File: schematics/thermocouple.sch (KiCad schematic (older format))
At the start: 0 parts

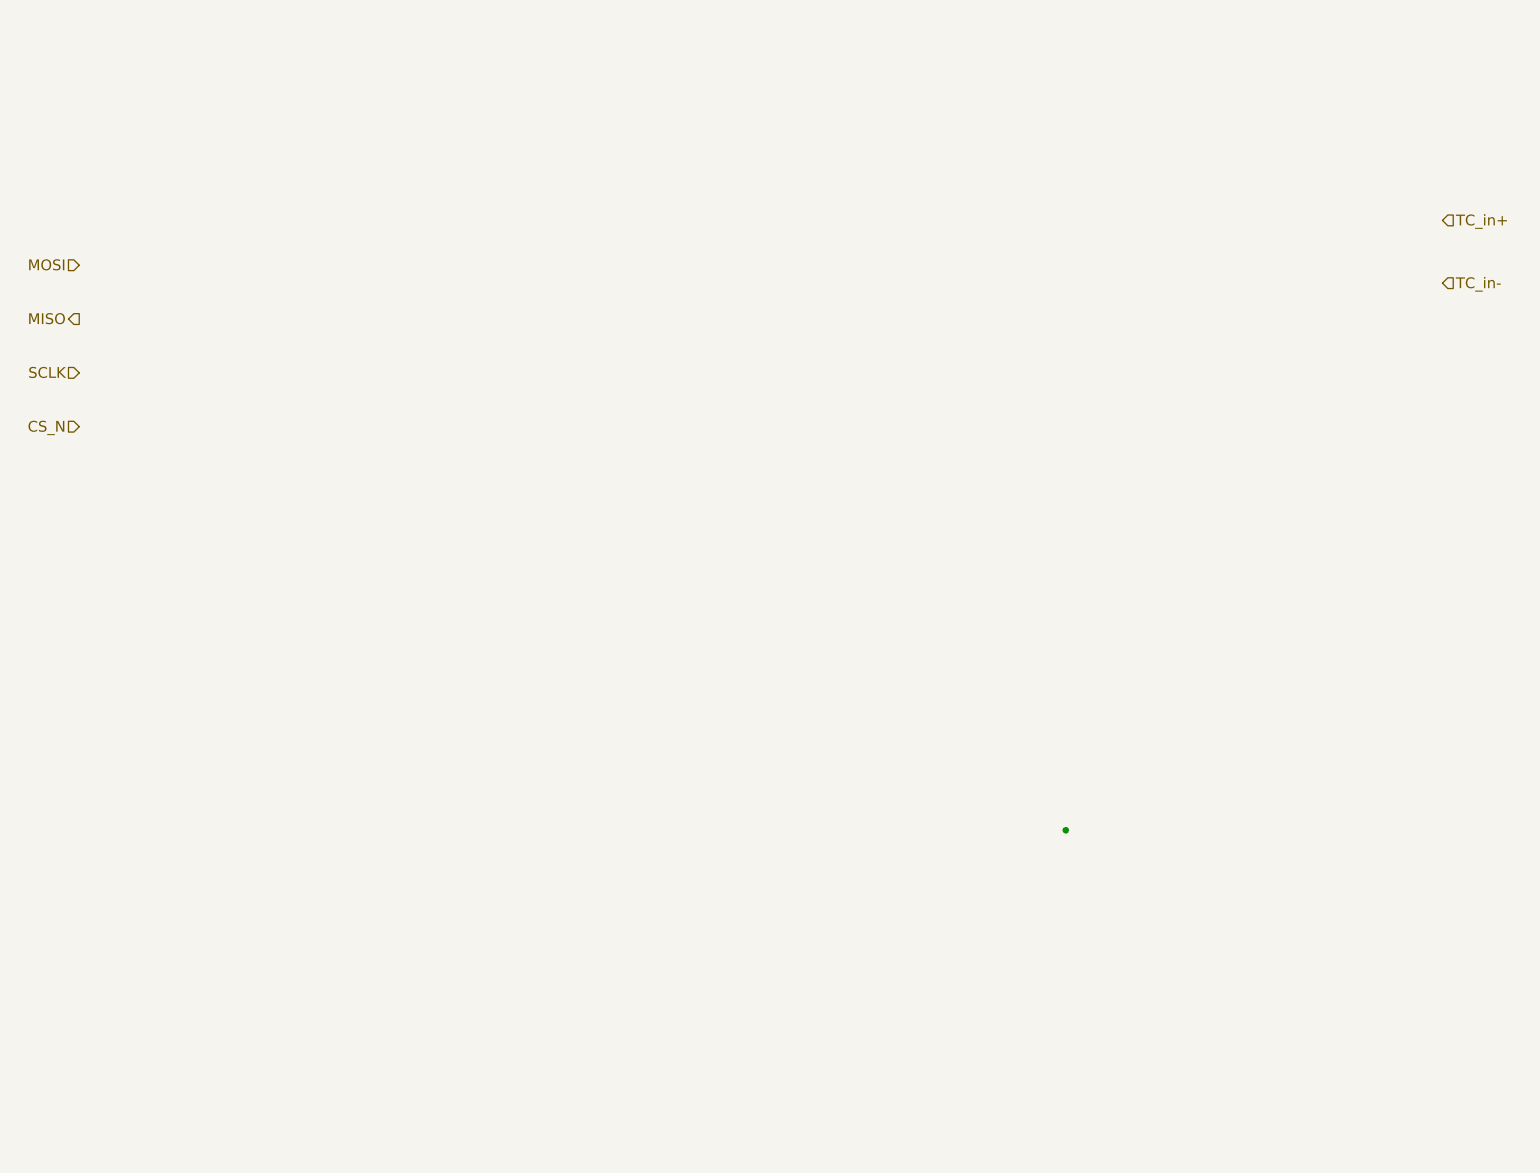
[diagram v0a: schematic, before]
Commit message: added fake diff amp and temp adc to thermocouple circuit
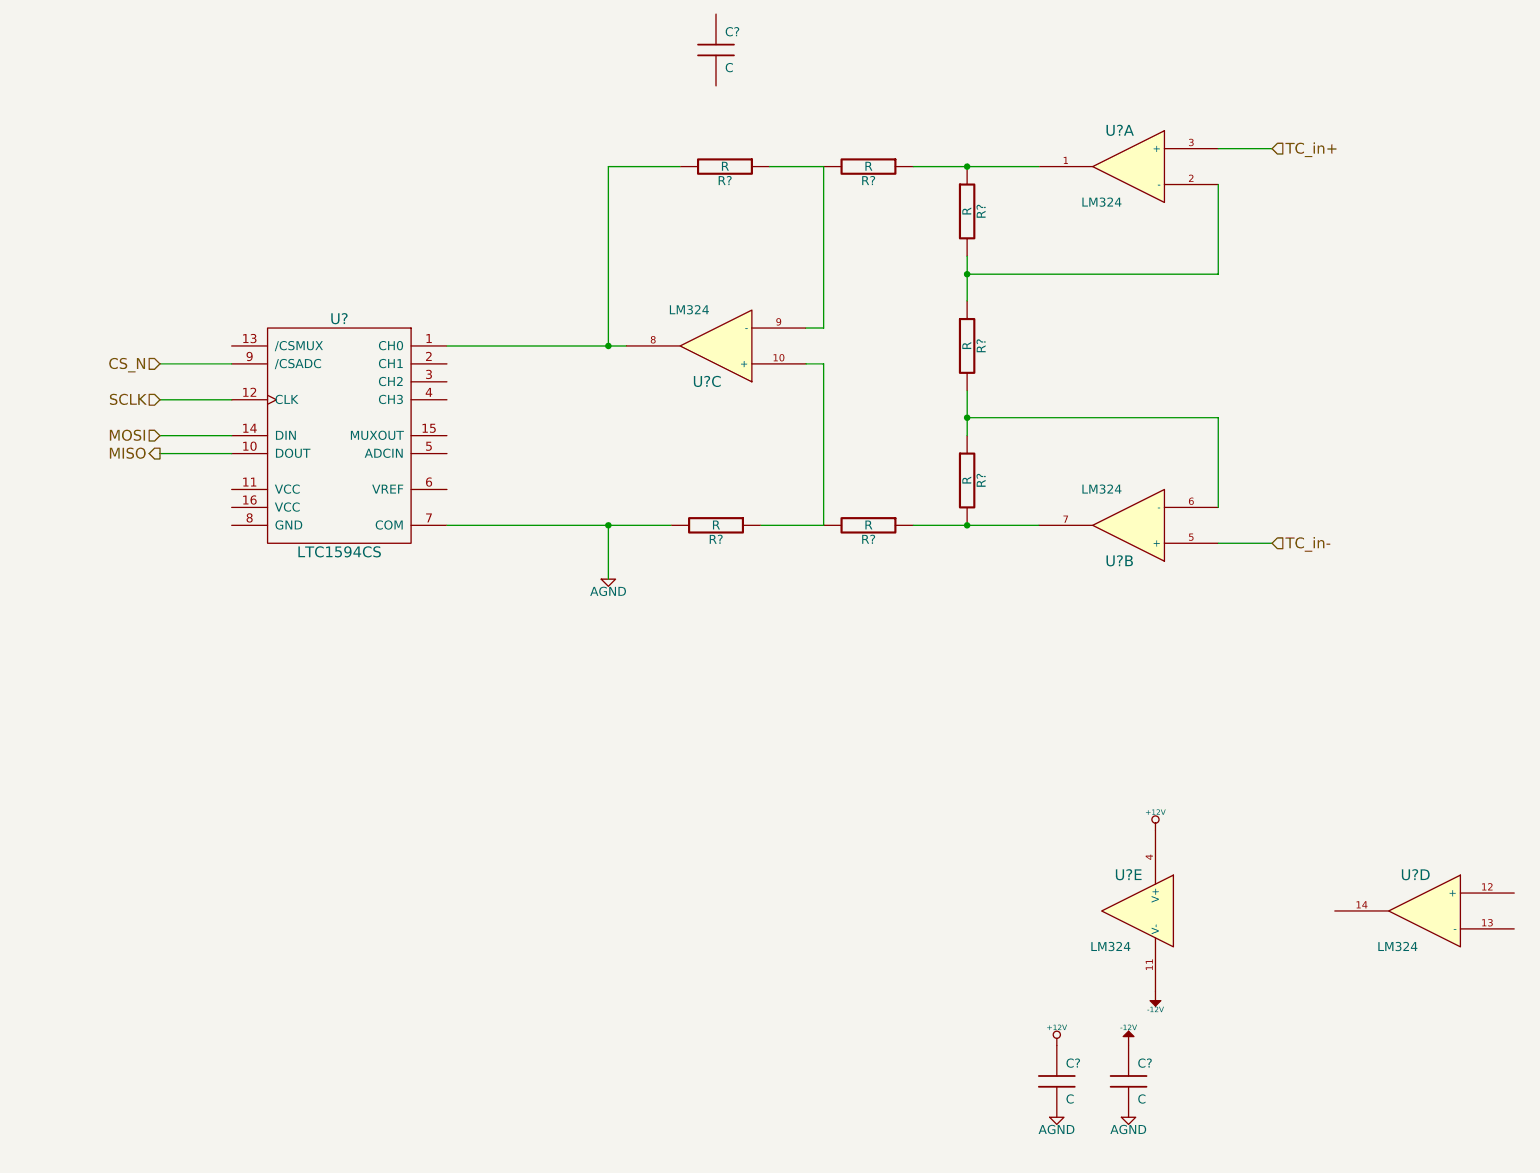
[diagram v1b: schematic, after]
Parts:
- added C? (x3): C, symbol C
- added R? (x7): R, symbol R
- added U? (x5): LM324, symbol LM324
- added U?: LTC1594CS, symbol LTC1594CS
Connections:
- net CS_N: now also U?.9 (/CSADC)
- net MISO: now also U?.10 (DOUT)
- net MOSI: now also U?.14 (DIN)
- net SCLK: now also U?.12 (CLK)
- net TC_in+: now also U?.3 (+)
- net TC_in-: now also U?.5 (+)
- new net: R?.1, R?.1, U?.1
- new net: R?.1, R?.2, U?.2 (-)
- new net: R?.1, R?.2, U?.10 (+)
- new net: R?.2, U?.1 (CH0), U?.8
- new net: R?.1, R?.2, U?.9 (-)
- new net: R?.1, R?.2, U?.6 (-)
- new net: R?.1, R?.2, U?.7
- new net +12V: C?.1, U?.4 (V+)
- new net -12V: C?.1, U?.11 (V-)
- new net AGND: C?.2, C?.2, R?.2, U?.7 (COM)

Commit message: added a temperature reference
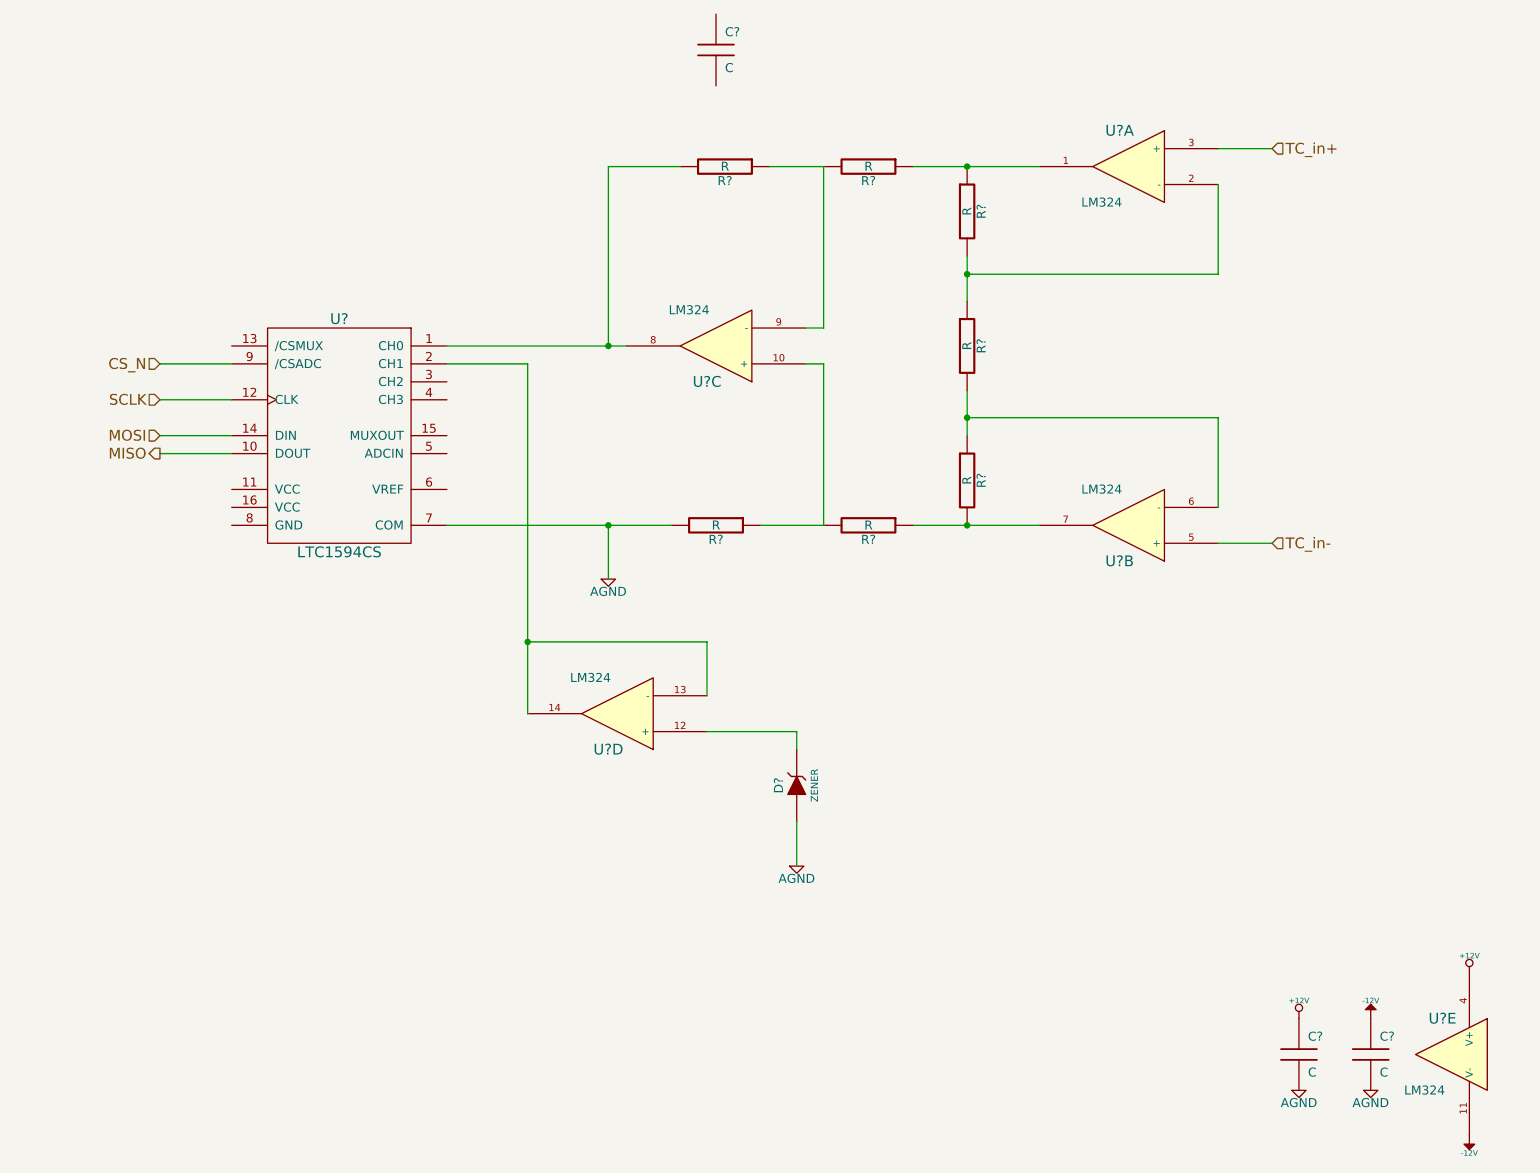
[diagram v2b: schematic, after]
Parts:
- added D?: ZENER, symbol ZENER
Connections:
- net AGND: now also D?.1 (A)
- net at U?.12 (+): now also D?.2 (K)
- net at U?.13 (-): now also U?.14, U?.2 (CH1)
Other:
- moved on the sheet: C?, U?D, U?E
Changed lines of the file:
@@
-EESchema Schematic File Version 2  date Sat 05 Oct 2013 09:08:15 PM EDT
+EESchema Schematic File Version 2  date Sat 05 Oct 2013 09:13:31 PM EDT
 LIBS:power
 LIBS:device
@@
 Comment4 ""
 $EndDescr
+Connection ~ 4050 4050
+Wire Wire Line
+	4050 4450 4050 2500
+Wire Wire Line
+	4050 2500 3600 2500
+Wire Wire Line
+	5050 4550 5550 4550
+Wire Wire Line
+	5550 4550 5550 4650
 Wire Wire Line
 	2000 2700 2400 2700
@@
 Wire Wire Line
 	2000 2900 2400 2900
+Wire Wire Line
+	5550 5300 5550 5050
+Wire Wire Line
+	5050 4350 5050 4050
+Wire Wire Line
+	5050 4050 4050 4050
+$Comp
+L AGND #PWR?
+U 1 1 5250B8B5
+P 5550 5300
+F 0 "#PWR?" H 5550 5300 40  0001 C CNN
+F 1 "AGND" H 5550 5230 50  0000 C CNN
+	1    5550 5300
+	1    0    0    -1
+$EndComp
+$Comp
+L ZENER D?
+U 1 1 5250B89E
+P 5550 4850
+F 0 "D?" H 5550 4950 50  0000 C CNN
+F 1 "ZENER" H 5550 4750 40  0000 C CNN
+	1    5550 4850
+	0    -1   -1   0
+$EndComp
 $Comp
 L LTC1594CS U?
@@
 L AGND #PWR?
 U 1 1 5250B6EC
-P 7000 6700
-F 0 "#PWR?" H 7000 6700 40  0001 C CNN
-F 1 "AGND" H 7000 6630 50  0000 C CNN
-	1    7000 6700
+P 8350 6550
+F 0 "#PWR?" H 8350 6550 40  0001 C CNN
+F 1 "AGND" H 8350 6480 50  0000 C CNN
+	1    8350 6550
 	1    0    0    -1
 $EndComp
@@
 L AGND #PWR?
 U 1 1 5250B6DC
-P 7400 6700
-F 0 "#PWR?" H 7400 6700 40  0001 C CNN
-F 1 "AGND" H 7400 6630 50  0000 C CNN
-	1    7400 6700
+P 8750 6550
+F 0 "#PWR?" H 8750 6550 40  0001 C CNN
+F 1 "AGND" H 8750 6480 50  0000 C CNN
+	1    8750 6550
 	1    0    0    -1
 $EndComp
@@
 L +12V #PWR?
 U 1 1 5250B670
-P 7000 6300
-F 0 "#PWR?" H 7000 6250 20  0001 C CNN
-F 1 "+12V" H 7000 6400 30  0000 C CNN
-	1    7000 6300
+P 8350 6150
+F 0 "#PWR?" H 8350 6100 20  0001 C CNN
+F 1 "+12V" H 8350 6250 30  0000 C CNN
+	1    8350 6150
 	1    0    0    -1
 $EndComp
@@
 L -12V #PWR?
 U 1 1 5250B662
-P 7400 6300
-F 0 "#PWR?" H 7400 6430 20  0001 C CNN
-F 1 "-12V" H 7400 6400 30  0000 C CNN
-	1    7400 6300
+P 8750 6150
+F 0 "#PWR?" H 8750 6280 20  0001 C CNN
+F 1 "-12V" H 8750 6250 30  0000 C CNN
+	1    8750 6150
 	1    0    0    -1
 $EndComp
@@
 L C C?
 U 1 1 5250B659
-P 7400 6500
-F 0 "C?" H 7450 6600 50  0000 L CNN
-F 1 "C" H 7450 6400 50  0000 L CNN
-	1    7400 6500
+P 8750 6350
+F 0 "C?" H 8800 6450 50  0000 L CNN
+F 1 "C" H 8800 6250 50  0000 L CNN
+	1    8750 6350
 	1    0    0    -1
 $EndComp
@@
 L C C?
 U 1 1 5250B64F
-P 7000 6500
-F 0 "C?" H 7050 6600 50  0000 L CNN
-F 1 "C" H 7050 6400 50  0000 L CNN
-	1    7000 6500
+P 8350 6350
+F 0 "C?" H 8400 6450 50  0000 L CNN
+F 1 "C" H 8400 6250 50  0000 L CNN
+	1    8350 6350
 	1    0    0    -1
 $EndComp
@@
 L +12V #PWR?
 U 1 1 5250B613
-P 7550 5100
-F 0 "#PWR?" H 7550 5050 20  0001 C CNN
-F 1 "+12V" H 7550 5200 30  0000 C CNN
-	1    7550 5100
+P 9300 5900
+F 0 "#PWR?" H 9300 5850 20  0001 C CNN
+F 1 "+12V" H 9300 6000 30  0000 C CNN
+	1    9300 5900
 	1    0    0    -1
 $EndComp
@@
 L -12V #PWR?
 U 1 1 5250B606
-P 7550 6000
-F 0 "#PWR?" H 7550 6130 20  0001 C CNN
-F 1 "-12V" H 7550 6100 30  0000 C CNN
-	1    7550 6000
+P 9300 6800
+F 0 "#PWR?" H 9300 6930 20  0001 C CNN
+F 1 "-12V" H 9300 6900 30  0000 C CNN
+	1    9300 6800
 	-1   0    0    1
 $EndComp
@@
 L LM324 U?
 U 5 1 5250B5D8
-P 7450 5550
-F 0 "U?" H 7500 5750 60  0000 C CNN
-F 1 "LM324" H 7600 5350 50  0000 C CNN
-	5    7450 5550
+P 9200 6350
+F 0 "U?" H 9250 6550 60  0000 C CNN
+F 1 "LM324" H 9350 6150 50  0000 C CNN
+	5    9200 6350
 	-1   0    0    -1
 $EndComp
@@
 L LM324 U?
 U 4 1 5250B13F
-P 9050 5550
-F 0 "U?" H 9100 5750 60  0000 C CNN
-F 1 "LM324" H 9200 5350 50  0000 C CNN
-	4    9050 5550
-	-1   0    0    -1
-$EndComp
-$Comp
+P 4550 4450
+F 0 "U?" H 4600 4650 60  0000 C CNN
+F 1 "LM324" H 4700 4250 50  0000 C CNN
+	4    4550 4450
+	-1   0    0    1
+$EndComp
+$Comp

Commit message: added comments to TC sch
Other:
- note added: "16-24bit ADC"
- note added: "Analog TC Input"
- note added: "General Temperauter Sensor"
- note added: "Instrumentation Amplifier Clone\n"
- moved on the sheet: C?
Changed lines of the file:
@@
-EESchema Schematic File Version 2  date Sat 05 Oct 2013 09:13:31 PM EDT
+EESchema Schematic File Version 2  date Sat 05 Oct 2013 09:15:56 PM EDT
 LIBS:power
 LIBS:device
@@
 Comment4 ""
 $EndDescr
+Text Notes 5400 850  0    60   ~ 0
+Instrumentation Amplifier Clone\n
+Text Notes 2800 1900 0    60   ~ 0
+16-24bit ADC
+Text Notes 8000 2400 0    60   ~ 0
+Analog TC Input
+Text Notes 5850 4800 0    60   ~ 0
+General Temperauter Sensor
 Connection ~ 4050 4050
 Wire Wire Line
@@
 L C C?
 U 1 1 5250B1A4
-P 5100 750
-F 0 "C?" H 5150 850 50  0000 L CNN
-F 1 "C" H 5150 650 50  0000 L CNN
-	1    5100 750
-	1    0    0    -1
-$EndComp
+P 3000 4000
+F 0 "C?" H 3050 4100 50  0000 L CNN
+F 1 "C" H 3050 3900 50  0000 L CNN
+	1    3000 4000
+	1    0    0    -1
+$EndComp
